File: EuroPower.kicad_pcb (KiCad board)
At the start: 2 copper layers, 200 x 95 mm, 17 parts, among them J1 Screw_Terminal_01x03, J2 Conn_02x05_Odd_Even, J3 Conn_02x05_Odd_Even, J4 Conn_02x05_Odd_Even, J5 Conn_02x05_Odd_Even, U1 LM7812_TO220, U2 LM7912_TO220

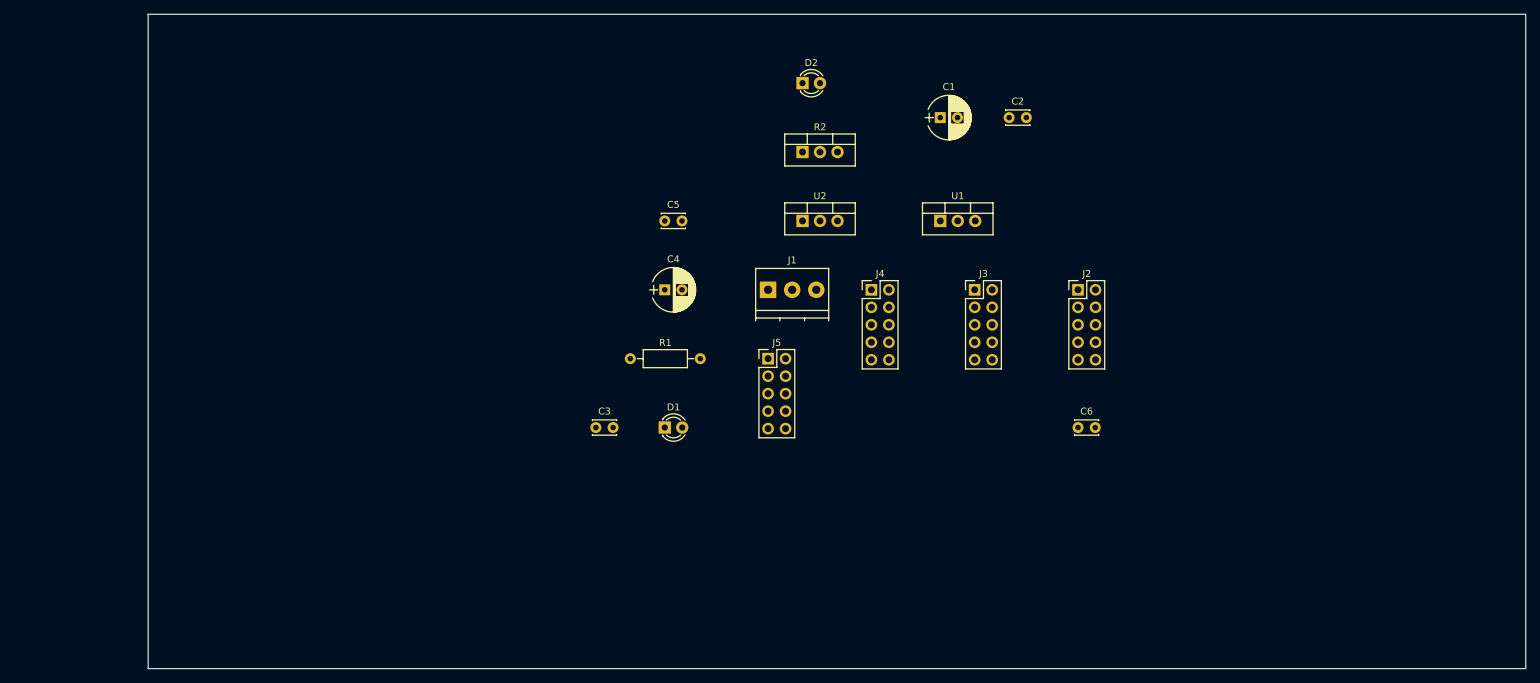
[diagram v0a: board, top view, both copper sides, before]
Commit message: Daisy-chainable design.
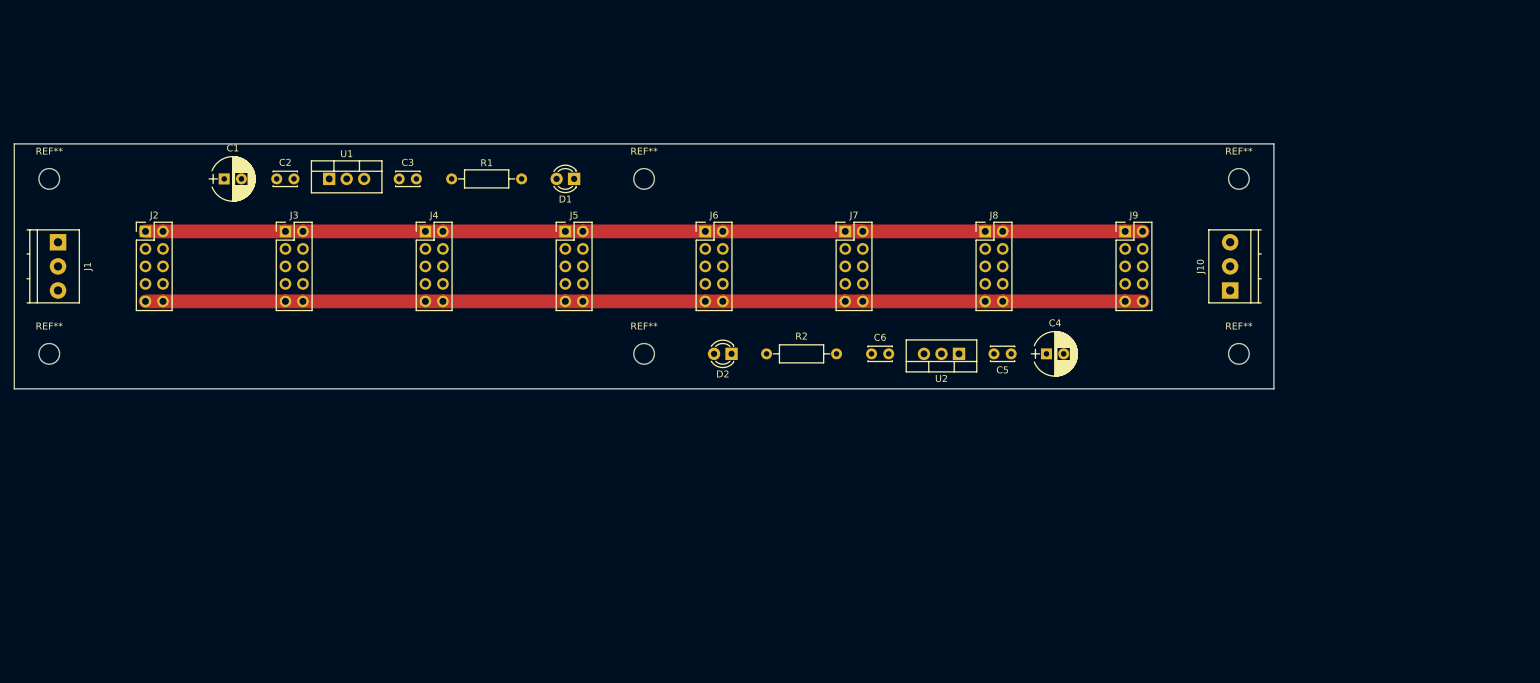
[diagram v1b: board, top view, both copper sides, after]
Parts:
- added J10: Screw_Terminal_01x03, TerminalBlocks_Phoenix:TerminalBlock_Phoenix_PT-3.5mm_3pol, F.Cu at (212.1, 105.1)
- added J6: Conn_02x05_Odd_Even, Pin_Headers:Pin_Header_Straight_2x05_Pitch2.54mm, F.Cu at (135.9, 96.5)
- added J7: Conn_02x05_Odd_Even, Pin_Headers:Pin_Header_Straight_2x05_Pitch2.54mm, F.Cu at (156.2, 96.5)
- added J8: Conn_02x05_Odd_Even, Pin_Headers:Pin_Header_Straight_2x05_Pitch2.54mm, F.Cu at (176.5, 96.5)
- added J9: Conn_02x05_Odd_Even, Pin_Headers:Pin_Header_Straight_2x05_Pitch2.54mm, F.Cu at (196.8, 96.5)
- added REF**: MountingHole_3mm, Mounting_Holes:MountingHole_3mm, F.Cu at (40.6, 88.9)
- added REF**: MountingHole_3mm, Mounting_Holes:MountingHole_3mm, F.Cu at (213.4, 114.3)
- added REF**: MountingHole_3mm, Mounting_Holes:MountingHole_3mm, F.Cu at (213.4, 88.9)
- added REF**: MountingHole_3mm, Mounting_Holes:MountingHole_3mm, F.Cu at (40.6, 114.3)
- added REF**: MountingHole_3mm, Mounting_Holes:MountingHole_3mm, F.Cu at (127.0, 88.9)
- added REF**: MountingHole_3mm, Mounting_Holes:MountingHole_3mm, F.Cu at (127.0, 114.3)
- R2: footprint TO_SOT_Packages_THT:TO-220-3_Vertical -> Resistors_THT:R_Axial_DIN0207_L6.3mm_D2.5mm_P10.16mm_Horizontal
- moved J2 135.7 mm to (54.6, 96.5)
- moved C2 106.7 mm to (73.7, 88.9)
- moved C1 104.3 mm to (66.0, 88.9)
- moved J1 103.3 mm to (41.9, 98.1), turned to 270 degrees
- moved J3 100.4 mm to (74.9, 96.5)
- moved U1 88.9 mm to (81.3, 88.9)
- moved J4 65.3 mm to (95.2, 96.5)
- moved C4 56.2 mm to (185.4, 114.3)
- moved C5 53.9 mm to (180.3, 114.3), turned to 180 degrees
- moved C3 46.0 mm to (91.4, 88.9)
- moved D2 40.6 mm to (139.7, 114.3), turned to 180 degrees
- moved D1 38.4 mm to (116.8, 88.9), turned to 180 degrees
- moved R1 36.8 mm to (99.1, 88.9)
- moved J5 34.8 mm to (115.6, 96.5)
- moved C6 31.8 mm to (160.0, 114.3)
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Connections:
- net Net-(C1-Pad2) renamed GND
- net Net-(C3-Pad1) renamed +12V
- net Net-(C6-Pad2) renamed -12V
- J1 pad 1: Net-(C4-Pad2) -> Net-(C1-Pad1)
- J1 pad 3: Net-(C1-Pad1) -> Net-(C4-Pad2)
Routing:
- net +12V: track 0.00 -> 146.0 mm
- net -12V: track 0.00 -> 144.8 mm
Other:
- board size 200 x 95 mm -> 182.9 x 35.6 mm

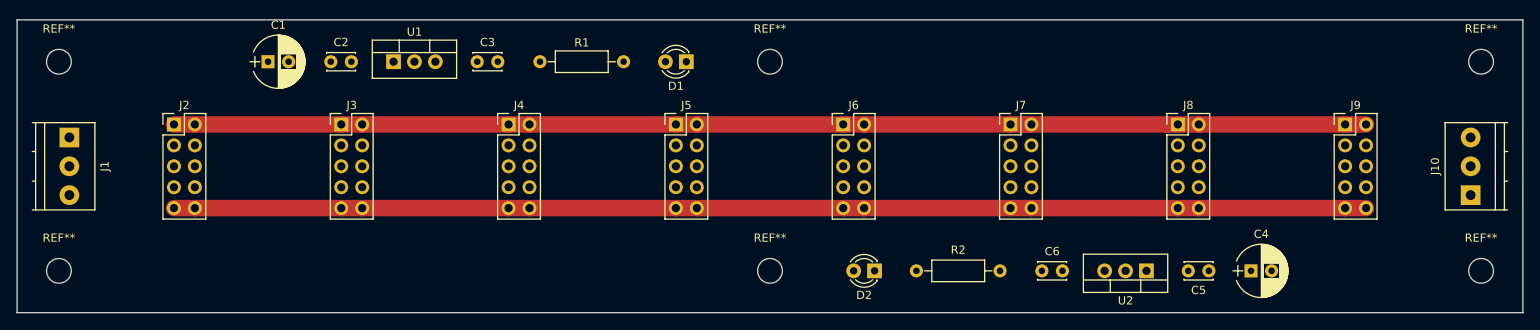
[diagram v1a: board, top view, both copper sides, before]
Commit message: Routed power lines.
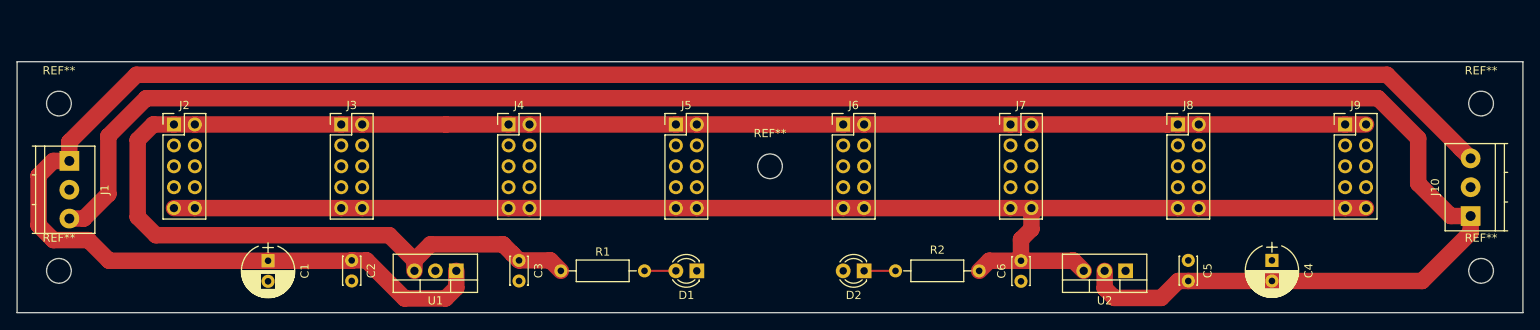
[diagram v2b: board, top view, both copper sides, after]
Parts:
- removed the REF** at (127.0, 114.3)
- moved U1 26.5 mm to (88.9, 114.3), turned to 180 degrees
- moved R1 25.5 mm to (101.6, 114.3)
- moved D1 25.4 mm to (118.1, 114.3)
- moved C3 24.7 mm to (96.5, 113.0), turned to 270 degrees
- moved C2 24.3 mm to (76.2, 113.0), turned to 270 degrees
- moved C1 24.2 mm to (66.0, 113.1), turned to 270 degrees
- moved REF** 12.7 mm to (127.0, 101.6)
- moved REF** 5.08 mm to (40.6, 94.0)
- moved REF** 5.08 mm to (213.4, 94.0)
- moved J1 2.85 mm to (41.9, 101.0)
- moved C4 2.84 mm to (188.0, 113.0), turned to 270 degrees
- moved C6 2.84 mm to (157.5, 115.6), turned to 90 degrees
- moved C5 2.80 mm to (177.8, 113.0), turned to 270 degrees
- moved J10 2.54 mm to (212.1, 107.6)
- moved R2 2.54 mm to (142.2, 114.3)
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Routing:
- net Net-(C1-Pad1): track 0.00 -> 247.6 mm
- net Net-(C4-Pad2): track 0.00 -> 241.8 mm
- net +12V: track 146.0 -> 217.6 mm
- net -12V: track 144.8 -> 165.4 mm
- net Net-(D2-Pad1): track 0.00 -> 3.81 mm
- net Net-(D1-Pad2): track 0.00 -> 3.81 mm
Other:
- board size 182.9 x 35.6 mm -> 182.9 x 30.5 mm
